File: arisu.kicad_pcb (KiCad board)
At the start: 2 copper layers, 339.1 x 118.7 mm, 176 parts, among them J1 USB_B_Micro, SW1 SW_Push, SW10 SW_Push, SW11 SW_Push, SW12 SW_Push, SW13 SW_Push, SW14 SW_Push, SW15 SW_Push, SW16 SW_Push, SW17 SW_Push, SW18 SW_Push, SW19 SW_Push, SW2 SW_Push, SW20 SW_Push, SW21 SW_Push, SW22 SW_Push, SW23 SW_Push, SW24 SW_Push, SW25 SW_Push, SW26 SW_Push, SW27 SW_Push, SW28 SW_Push, SW29 SW_Push, SW3 SW_Push, SW30 SW_Push, SW31 SW_Push, SW32 SW_Push, SW33 SW_Push, SW34 SW_Push, SW35 SW_Push, SW36 SW_Push, SW37 SW_Push, SW38 SW_Push, SW39 SW_Push, SW4 SW_Push, SW40 SW_Push, SW41 SW_Push, SW42 SW_Push, SW43 SW_Push, SW44 SW_Push, SW45 SW_Push, SW46 SW_Push, SW47 SW_Push, SW48 SW_Push, SW49 SW_Push, SW5 SW_Push, SW50 SW_Push, SW51 SW_Push, SW52 SW_Push, SW53 SW_Push, SW54 SW_Push, SW55 SW_Push, SW56 SW_Push, SW57 SW_Push, SW58 SW_Push, SW59 SW_Push, SW6 SW_Push, SW60 SW_Push, SW61 SW_Push, SW62 SW_Push, SW63 SW_Push, SW64 SW_Push, SW65 SW_Push, SW66 SW_Push, SW67 SW_Push, SW7 SW_Push, SW8 SW_Push, SW9 SW_Push, U1 USBLC6-2SC6, U2 ATmega32U4-AU, Y1 Crystal_GND24

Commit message: Begin reworking PCB layout with removed top row.
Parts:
- removed D1, D10, D15, D19, D24, D29, D33, D38, D42, D47, D51, D55, D59, D6, D63: D, Diodes_SMD:D_SOD-123
- removed G*** (x2): LOGO, arisu:arisu-logo
- removed SW1, SW10, SW15, SW19, SW24, SW29, SW33, SW38, SW42, SW47, SW51, SW55, SW59, SW6, SW63: SW_Push, Fate_Parts:SW_Cherry_MX_1.00u_PCB
- renumbered PF6 to J10, PF7 to J11, VCC to J12, D+ to J13, D- to J14, GND to J15, MISO to J2, VCC to J3, SCK to J4, MOSI to J5, RES to J6, GND to J7, PF4 to J8, PF5 to J9
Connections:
- D11 pad 1: /row1 -> /row0
- D12 pad 1: /row2 -> /row1
- D13 pad 1: /row3 -> /row2
- D14 pad 1: /row4 -> /row3
- D16 pad 1: /row1 -> /row0
- D17 pad 1: /row2 -> /row1
- D18 pad 1: /row3 -> /row2
- D2 pad 1: /row1 -> /row0
- D20 pad 1: /row1 -> /row0
- D21 pad 1: /row2 -> /row1
- D22 pad 1: /row3 -> /row2
- D23 pad 1: /row4 -> /row3
- D25 pad 1: /row1 -> /row0
- D26 pad 1: /row2 -> /row1
- D27 pad 1: /row3 -> /row2
- D28 pad 1: /row4 -> /row3
- D3 pad 1: /row2 -> /row1
- D30 pad 1: /row1 -> /row0
- D31 pad 1: /row2 -> /row1
- D32 pad 1: /row3 -> /row2
- D34 pad 1: /row1 -> /row0
- D35 pad 1: /row2 -> /row1
- D36 pad 1: /row3 -> /row2
- D37 pad 1: /row4 -> /row3
- D39 pad 1: /row1 -> /row0
- D4 pad 1: /row3 -> /row2
- D40 pad 1: /row2 -> /row1
- D41 pad 1: /row3 -> /row2
- D43 pad 1: /row1 -> /row0
- D44 pad 1: /row2 -> /row1
- D45 pad 1: /row3 -> /row2
- D46 pad 1: /row4 -> /row3
- D48 pad 1: /row1 -> /row0
- D49 pad 1: /row2 -> /row1
- D5 pad 1: /row4 -> /row3
- D50 pad 1: /row3 -> /row2
- D52 pad 1: /row1 -> /row0
- D53 pad 1: /row2 -> /row1
- D54 pad 1: /row3 -> /row2
- D56 pad 1: /row1 -> /row0
- D57 pad 1: /row2 -> /row1
- D58 pad 1: /row4 -> /row3
- D60 pad 1: /row1 -> /row0
- D61 pad 1: /row3 -> /row2
- D62 pad 1: /row4 -> /row3
- D64 pad 1: /row1 -> /row0
- D65 pad 1: /row2 -> /row1
- D66 pad 1: /row3 -> /row2
- D67 pad 1: /row4 -> /row3
- D7 pad 1: /row1 -> /row0
- D8 pad 1: /row2 -> /row1
- D9 pad 1: /row3 -> /row2
- U2 pad 22: /row4 -> Net-(U2-Pad22)
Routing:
- net Net-(D42-Pad2): track 5.08 -> 0.00 mm
- net Net-(D38-Pad2): track 5.08 -> 0.00 mm
- net Net-(D33-Pad2): track 5.08 -> 0.00 mm
- net Net-(D47-Pad2): track 5.08 -> 0.00 mm
- net Net-(D51-Pad2): track 4.91 -> 0.00 mm
- net Net-(D10-Pad2): track 4.91 -> 0.00 mm
- net Net-(D6-Pad2): track 4.91 -> 0.00 mm
- net Net-(D1-Pad2): track 4.91 -> 0.00 mm
- net Net-(D63-Pad2): track 4.91 -> 0.00 mm
- net Net-(D59-Pad2): track 4.91 -> 0.00 mm
- net Net-(D55-Pad2): track 4.91 -> 0.00 mm
- net Net-(D29-Pad2): track 4.85 -> 0.00 mm
- net Net-(D24-Pad2): track 4.85 -> 0.00 mm
- net Net-(D19-Pad2): track 4.85 -> 0.00 mm
- net Net-(D15-Pad2): track 4.85 -> 0.00 mm
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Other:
- board text added: "Faux Design Rev 0.0.0"
- board text removed: "Fate Design Rev 1.1"

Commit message: Redesign alpha layout for natural finger spread.
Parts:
- removed D60, D64, D65, D66, D67: D, Diodes_SMD:D_SOD-123
- removed SW60: SW_Push, Fate_Parts:SW_Cherry_MX_1.50u_PCB
- removed SW64, SW65, SW66, SW67: SW_Push, Fate_Parts:SW_Cherry_MX_1.00u_PCB
- moved SW25 160.0 mm to (162.0, 217.3), turned to 344 degrees
- moved D25 159.9 mm to (164.0, 231.6), turned to 74 degrees
- moved SW20 158.8 mm to (143.7, 212.1), turned to 344 degrees
- moved D20 158.8 mm to (147.1, 226.4), turned to 74 degrees
- moved SW30 157.1 mm to (192.0, 222.6), turned to 16 degrees
- moved D30 156.6 mm to (201.7, 233.6), turned to 106 degrees
- moved SW31 156.0 mm to (206.4, 238.3), turned to 16 degrees
- moved SW34 155.8 mm to (210.3, 217.3), turned to 16 degrees
- moved D34 155.7 mm to (220.1, 228.8), turned to 106 degrees
- moved D26 155.2 mm to (150.1, 247.7), turned to 74 degrees
- moved D32 155.1 mm to (229.7, 265.6), turned to 106 degrees
- moved SW32 155.1 mm to (220.8, 253.9), turned to 16 degrees
- moved D31 155.0 mm to (216.2, 248.8), turned to 106 degrees
- moved SW26 154.8 mm to (147.6, 233.0), turned to 344 degrees
- moved D35 154.8 mm to (234.2, 244.7), turned to 106 degrees
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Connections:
- J1 pad 4: Net-(J1-Pad4) -> (no net)
- SW61 pad 1: /col13 -> /col12
- SW62 pad 1: /col13 -> /col11
- U1 pad 1: Net-(U1-Pad1) -> (no net)
- U1 pad 3: Net-(U1-Pad3) -> (no net)
- U2 pad 22: Net-(U2-Pad22) -> (no net)
- U2 pad 26: /col13 -> (no net)
- U2 pad 42: Net-(U2-Pad42) -> (no net)
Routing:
- net /row4: track 433.8 -> 0.00 mm, vias 2 -> 0
- net /row3: track 432.5 -> 0.00 mm, vias 2 -> 0
- net /row2: track 399.4 -> 0.00 mm, vias 4 -> 0
- net /row1: track 384.1 -> 0.00 mm, vias 4 -> 0
- net /row0: track 328.0 -> 0.00 mm, vias 4 -> 0
- net /MISO: track 272.2 -> 0.00 mm, vias 1 -> 0
- net /col13: track 269.0 -> 0.00 mm
- net /col12: track 249.0 -> 0.00 mm
- net /col11: track 230.6 -> 0.00 mm
- net /col10: track 221.3 -> 0.00 mm
- net VCC: track 205.4 -> 0.00 mm, vias 9 -> 0
- net /col0: track 204.9 -> 0.00 mm, vias 1 -> 0
- net /col2: track 175.7 -> 0.00 mm, vias 2 -> 0
- net /col1: track 166.8 -> 0.00 mm
- net /SCK: track 157.0 -> 0.00 mm, vias 2 -> 0
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
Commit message: Continue making symmetrical layout.
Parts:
- moved D28 158.5 mm to (149.7, 292.2)
- moved SW28 158.5 mm to (146.3, 277.9)
- moved D46 157.6 mm to (272.3, 278.3)
- moved SW37 157.6 mm to (207.4, 278.5)
- moved SW46 157.6 mm to (258.7, 267.6)
- moved D37 157.6 mm to (232.7, 286.7)
- moved SW23 157.5 mm to (105.4, 268.8)
- moved D23 157.5 mm to (118.2, 285.1)
- moved SW14 151.4 mm to (47.1, 251.8), turned to 0 degrees
- moved D11 150.3 mm to (97.7, 211.1)
- moved SW11 150.3 mm to (94.3, 196.8)
- moved D16 150.3 mm to (116.4, 215.1)
- moved SW16 150.3 mm to (113.0, 200.8)
- moved D14 148.9 mm to (57.7, 265.2), turned to 90 degrees
- moved D12 148.0 mm to (89.1, 228.8)
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
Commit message: Make 69 spacebar layout lol.
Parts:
- removed D61: D, Diodes_SMD:D_SOD-123
- removed SW61: SW_Push, Fate_Parts:SW_Cherry_MX_1.00u_PCB
- added D63: D, Diode_SMD:D_SOD-123, B.Cu at (348.3, 111.3)
- added D64: D, Diode_SMD:D_SOD-123, F.Cu at (375.0, 54.8)
- added D69: D, Diode_SMD:D_SOD-123, F.Cu at (203.6, 154.8)
- added SW63: SW_Push, MX_Switch:SW_Cherry_MX_1.00u_PCB, F.Cu at (342.4, 98.3)
- added SW64: SW_Push, MX_Switch:SW_Cherry_MX_1.00u_PCB, F.Cu at (369.4, 41.1)
- added SW69: SW_Push, Button_Switch_Keyboard:SW_Cherry_MX_6.25u_PCB, F.Cu at (209.6, 146.4)
- SW11, SW12, SW13, SW16, SW17, SW18, SW20, SW21, SW22, SW25, SW26, SW27, SW30, SW31, SW32, SW34, SW35, SW36, SW39, SW40, SW41, SW43, SW44, SW45, SW48, SW49, SW50, SW52, SW53, SW56, SW7, SW8, SW9: footprint Fate_Parts:SW_Cherry_MX_1.00u_PCB -> MX_Switch:SW_Cherry_MX_1.00u_PCB
- SW14, SW2, SW46, SW5: footprint Fate_Parts:SW_Cherry_MX_1.50u_PCB -> MX_Switch:SW_Cherry_MX_1.50u_PCB
- SW23: footprint Fate_Parts:SW_Cherry_MX_2.00u_PCB_ReversedStabilizers -> MX_Switch:SW_Cherry_MX_1.00u_PCB
- SW28: footprint Fate_Parts:SW_Cherry_MX_1.00u_PCB -> MX_Switch:SW_Cherry_MX_2.25u_PCB_ReversedStabilizers
- SW3: footprint Fate_Parts:SW_Cherry_MX_1.75u_PCB -> MX_Switch:SW_Cherry_MX_1.75u_PCB
- SW37: footprint Fate_Parts:SW_Cherry_MX_2.75u_PCB_ReversedStabilizers -> MX_Switch:SW_Cherry_MX_2.25u_PCB_ReversedStabilizers
- SW4: footprint Fate_Parts:SW_Cherry_MX_2.25u_PCB -> MX_Switch:SW_Cherry_MX_2.25u_PCB
- SW54: footprint Fate_Parts:SW_Cherry_MX_1.75u_PCB -> MX_Switch:SW_Cherry_MX_2.75u_PCB
- SW57: footprint Fate_Parts:SW_Cherry_MX_2.25u_PCB_ReversedStabilizers -> MX_Switch:SW_Cherry_MX_2.25u_PCB_ReversedStabilizers
- SW58, SW62: footprint Fate_Parts:SW_Cherry_MX_1.00u_PCB -> MX_Switch:SW_Cherry_MX_1.50u_PCB
- moved SW28 163.9 mm to (148.8, 114.0)
- moved D28 162.1 mm to (163.1, 130.7)
- moved D23 161.5 mm to (133.8, 124.3)
- moved SW23 160.7 mm to (130.2, 110.0)
- moved D54 157.4 mm to (360.8, 92.5)
- moved SW37 156.0 mm to (219.6, 122.9)
- moved D12 155.9 mm to (108.2, 74.0)
- moved D13 155.9 mm to (99.6, 91.6)
- moved D14 155.9 mm to (76.8, 110.4)
- moved D16 155.9 mm to (135.4, 60.3)
- moved D17 155.9 mm to (126.8, 78.0)
- moved D18 155.9 mm to (118.2, 95.6)
- moved D2 155.9 mm to (61.9, 53.1)
- moved D20 155.9 mm to (164.3, 71.6)
- moved D21 155.9 mm to (150.5, 87.3)
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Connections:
- SW46 pad 1: /col9 -> /col8
- SW62 pad 1: /col11 -> /col9
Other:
- board size 339.1 x 118.7 mm -> 373.1 x 131.8 mm
- board text added: "Faux Keebs Rev 0.0.0"
- board text removed: "Faux Design Rev 0.0.0"

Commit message: Make it even MORE symmetrical!
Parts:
- removed D69: D, Diode_SMD:D_SOD-123
- removed SW69: SW_Push, Button_Switch_Keyboard:SW_Cherry_MX_6.25u_PCB
- moved H6 51.9 mm to (226.2, 131.0)
- moved H4 44.2 mm to (184.5, 131.0)
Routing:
- net /SCK: track 0.00 -> 105.4 mm
- net /col2: track 0.00 -> 89.6 mm
- net /col12: track 0.00 -> 86.2 mm
- net /col8: track 0.00 -> 86.1 mm
- net /col10: track 0.00 -> 84.0 mm
- net /col5: track 0.00 -> 82.3 mm
- net /col9: track 0.00 -> 81.7 mm
- net /col4: track 0.00 -> 81.0 mm
- net /col0: track 0.00 -> 80.1 mm
- net /col1: track 0.00 -> 53.3 mm
- net /col3: track 0.00 -> 52.1 mm
- net /col11: track 0.00 -> 50.9 mm
- net /col6: track 0.00 -> 47.2 mm
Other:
- board size 373.1 x 131.8 mm -> 373.1 x 110.3 mm

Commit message: Route more row tracks.
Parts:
- moved D64 0.89 mm to (375.9, 54.6)
- moved D58 0.65 mm to (372.1, 111.6)
- turned D63 to 90 degrees
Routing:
- net /row1: track 0.00 -> 373.1 mm
- net /row3: track 0.00 -> 370.3 mm
- net /row0: track 0.00 -> 349.7 mm
- net Net-(D32-Pad2): track 0.00 -> 5.79 mm
- net Net-(D36-Pad2): track 0.00 -> 5.74 mm
- net Net-(D35-Pad2): track 0.00 -> 5.64 mm
- net Net-(D22-Pad2): track 0.00 -> 5.36 mm
- net Net-(D44-Pad2): track 0.00 -> 5.33 mm
- net Net-(D37-Pad2): track 0.00 -> 5.27 mm
- net Net-(D34-Pad2): track 0.00 -> 5.24 mm
- net Net-(D41-Pad2): track 0.00 -> 5.23 mm
- net Net-(D64-Pad2): track 0.00 -> 5.23 mm
- net Net-(D43-Pad2): track 0.00 -> 5.21 mm
- net Net-(D30-Pad2): track 0.00 -> 5.11 mm
- net Net-(D26-Pad2): track 0.00 -> 5.09 mm
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
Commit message: Finish routing rows.
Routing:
- net /row2: track 0.00 -> 420.6 mm
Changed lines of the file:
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@@
     (thickness 1.6)
     (drawings 1381)
-    (tracks 397)
+    (tracks 458)
     (zones 0)
     (modules 136)
@@
   (segment (start 56.384333 66.445157) (end 55.799333 65.860157) (width 0.25) (layer B.Cu) (net 9))
   (segment (start 56.384333 70.525157) (end 56.384333 66.445157) (width 0.25) (layer B.Cu) (net 9))
+  (segment (start 375.92 65.172491) (end 375.92 56.26) (width 0.25) (layer B.Cu) (net 10))
+  (segment (start 123.19 101.6) (end 127 104.14) (width 0.25) (layer B.Cu) (net 10))
+  (segment (start 79.410583 92.875157) (end 79.410583 93.575157) (width 0.25) (layer B.Cu) (net 10))
+  (segment (start 378.46 67.712491) (end 375.92 65.172491) (width 0.25) (layer B.Cu) (net 10))
+  (segment (start 378.46 85.09) (end 378.46 67.712491) (width 0.25) (layer B.Cu) (net 10))
+  (segment (start 79.410583 93.575157) (end 81.085426 95.25) (width 0.25) (layer B.Cu) (net 10))
+  (segment (start 269.24 109.22) (end 280.93211 105.14789) (width 0.25) (layer B.Cu) (net 10))
+  (segment (start 345.44 96.52) (end 348.903637 93.633637) (width 0.25) (layer B.Cu) (net 10))
+  (segment (start 359.41 96.52) (end 369.57 96.52) (width 0.25) (layer B.Cu) (net 10))
+  (segment (start 348.903637 93.633637) (end 356.523637 93.633637) (width 0.25) (layer B.Cu) (net 10))
+  (segment (start 356.523637 93.633637) (end 359.41 96.52) (width 0.25) (layer B.Cu) (net 10))
+  (segment (start 369.57 96.52) (end 378.46 85.09) (width 0.25) (layer B.Cu) (net 10))
+  (segment (start 360.76089 95.16911) (end 359.41 96.52) (width 0.25) (layer B.Cu) (net 10))
+  (segment (start 360.76089 94.151218) (end 360.76089 95.16911) (width 0.25) (layer B.Cu) (net 10))
+  (segment (start 324.706479 94.151218) (end 322.337697 96.52) (width 0.25) (layer B.Cu) (net 10))
+  (segment (start 324.856479 94.151218) (end 324.706479 94.151218) (width 0.25) (layer B.Cu) (net 10))
+  (segment (start 322.337697 96.52) (end 320.04 96.52) (width 0.25) (layer B.Cu) (net 10))
+  (segment (start 320.04 96.52) (end 323.85 96.52) (width 0.25) (layer B.Cu) (net 10))
+  (segment (start 318.77 96.52) (end 323.85 96.52) (width 0.25) (layer B.Cu) (net 10))
+  (segment (start 323.85 96.52) (end 345.44 96.52) (width 0.25) (layer B.Cu) (net 10))
+  (segment (start 306.215179 96.086687) (end 308.899246 98.770754) (width 0.25) (layer B.Cu) (net 10))
+  (segment (start 304.611595 96.086687) (end 306.215179 96.086687) (width 0.25) (layer B.Cu) (net 10))
+  (segment (start 308.899246 98.770754) (end 318.77 96.52) (width 0.25) (layer B.Cu) (net 10))
+  (segment (start 285.977885 103.764403) (end 285.676144 104.066144) (width 0.25) (layer B.Cu) (net 10))
+  (segment (start 285.977885 100.047407) (end 285.977885 103.764403) (width 0.25) (layer B.Cu) (net 10))
+  (segment (start 280.93211 105.14789) (end 285.676144 104.066144) (width 0.25) (layer B.Cu) (net 10))
+  (segment (start 285.676144 104.066144) (end 308.899246 98.770754) (width 0.25) (layer B.Cu) (net 10))
+  (segment (start 265.229474 109.284883) (end 265.229474 110.289474) (width 0.25) (layer B.Cu) (net 10))
+  (segment (start 267.117263 107.397094) (end 265.229474 109.284883) (width 0.25) (layer B.Cu) (net 10))
+  (segment (start 267.841442 107.397094) (end 267.117263 107.397094) (width 0.25) (layer B.Cu) (net 10))
+  (segment (start 250.19 114.3) (end 265.229474 110.289474) (width 0.25) (layer B.Cu) (net 10))
+  (segment (start 265.229474 110.289474) (end 269.24 109.22) (width 0.25) (layer B.Cu) (net 10))
+  (segment (start 248.92 113.32333) (end 248.92 114.3) (width 0.25) (layer B.Cu) (net 10))
+  (segment (start 249.234402 113.008928) (end 248.92 113.32333) (width 0.25) (layer B.Cu) (net 10))
+  (segment (start 249.234402 112.440794) (end 249.234402 113.008928) (width 0.25) (layer B.Cu) (net 10))
+  (segment (start 162.56 114.3) (end 248.92 114.3) (width 0.25) (layer B.Cu) (net 10))
+  (segment (start 248.92 114.3) (end 250.19 114.3) (width 0.25) (layer B.Cu) (net 10))
+  (segment (start 153.733802 111.696198) (end 153.67 111.76) (width 0.25) (layer B.Cu) (net 10))
+  (segment (start 153.733802 109.821239) (end 153.733802 111.696198) (width 0.25) (layer B.Cu) (net 10))
+  (segment (start 153.67 111.76) (end 162.56 114.3) (width 0.25) (layer B.Cu) (net 10))
+  (segment (start 133.492318 105.267682) (end 132.926667 105.833333) (width 0.25) (layer B.Cu) (net 10))
+  (segment (start 134.57291 105.267682) (end 133.492318 105.267682) (width 0.25) (layer B.Cu) (net 10))
+  (segment (start 135.007432 104.83316) (end 134.57291 105.267682) (width 0.25) (layer B.Cu) (net 10))
+  (segment (start 127 104.14) (end 132.926667 105.833333) (width 0.25) (layer B.Cu) (net 10))
+  (segment (start 132.926667 105.833333) (end 153.67 111.76) (width 0.25) (layer B.Cu) (net 10))
+  (segment (start 118.11 98.051624) (end 118.11 100.33) (width 0.25) (layer B.Cu) (net 10))
+  (segment (start 117.837529 97.779153) (end 118.11 98.051624) (width 0.25) (layer B.Cu) (net 10))
+  (segment (start 117.837529 97.219101) (end 117.837529 97.779153) (width 0.25) (layer B.Cu) (net 10))
+  (segment (start 97.79 95.25) (end 118.11 100.33) (width 0.25) (layer B.Cu) (net 10))
+  (segment (start 118.11 100.33) (end 123.19 101.6) (width 0.25) (layer B.Cu) (net 10))
+  (segment (start 97.21663 95.25) (end 96.52 95.25) (width 0.25) (layer B.Cu) (net 10))
+  (segment (start 99.207529 93.259101) (end 97.21663 95.25) (width 0.25) (layer B.Cu) (net 10))
+  (segment (start 81.085426 95.25) (end 96.52 95.25) (width 0.25) (layer B.Cu) (net 10))
+  (segment (start 96.52 95.25) (end 97.79 95.25) (width 0.25) (layer B.Cu) (net 10))
+  (segment (start 81.085426 95.25) (end 68.58 95.25) (width 0.25) (layer B.Cu) (net 10))
+  (segment (start 68.58 95.25) (end 64.77 91.44) (width 0.25) (layer B.Cu) (net 10))
+  (segment (start 64.77 91.44) (end 60.96 91.44) (width 0.25) (layer B.Cu) (net 10))
+  (segment (start 60.96 91.44) (end 57.15 95.25) (width 0.25) (layer B.Cu) (net 10))
+  (segment (start 57.15 95.25) (end 49.53 95.25) (width 0.25) (layer B.Cu) (net 10))
+  (segment (start 48.456833 94.176833) (end 48.456833 92.875157) (width 0.25) (layer B.Cu) (net 10))
+  (segment (start 49.53 95.25) (end 48.456833 94.176833) (width 0.25) (layer B.Cu) (net 10))
   (segment (start 48.606833 111.925157) (end 50.981676 114.3) (width 0.25) (layer B.Cu) (net 11))
   (segment (start 48.456833 111.925157) (end 48.606833 111.925157) (width 0.25) (layer B.Cu) (net 11))

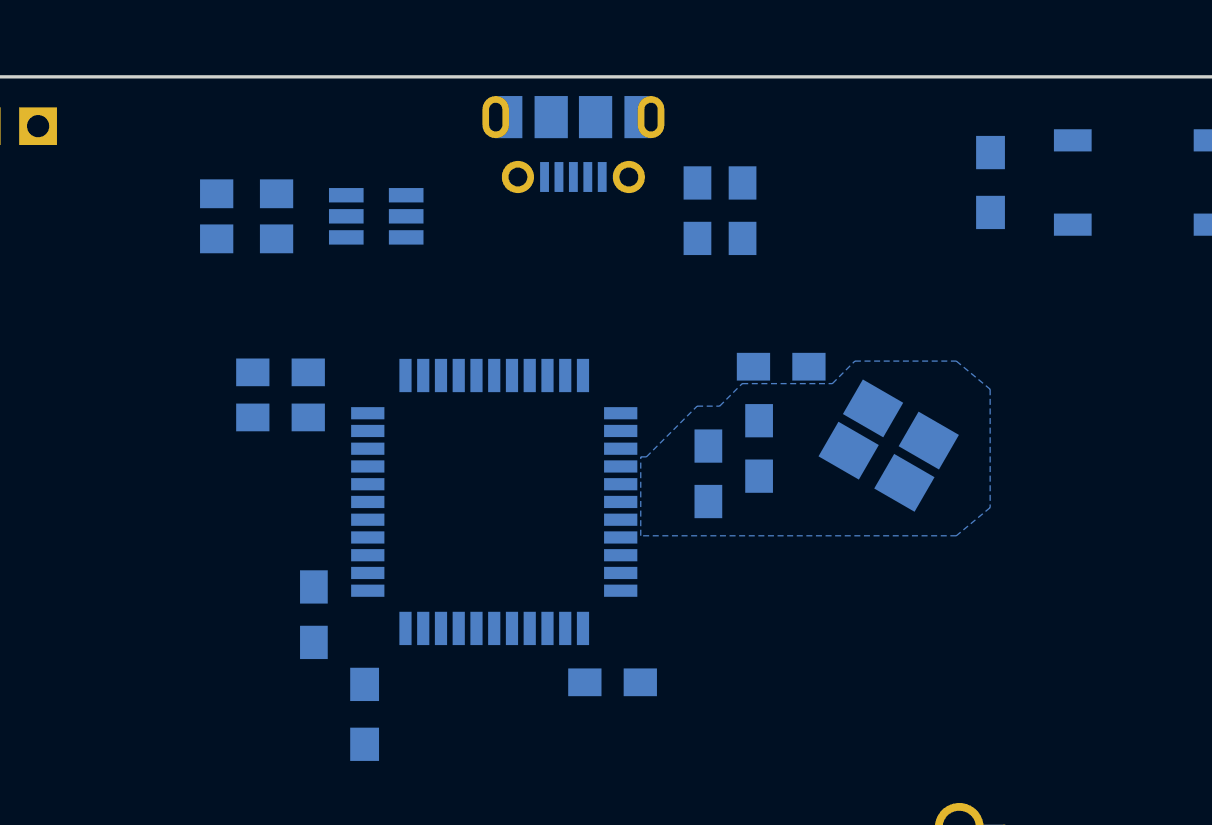
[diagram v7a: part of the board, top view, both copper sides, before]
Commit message: Route some of the central components.
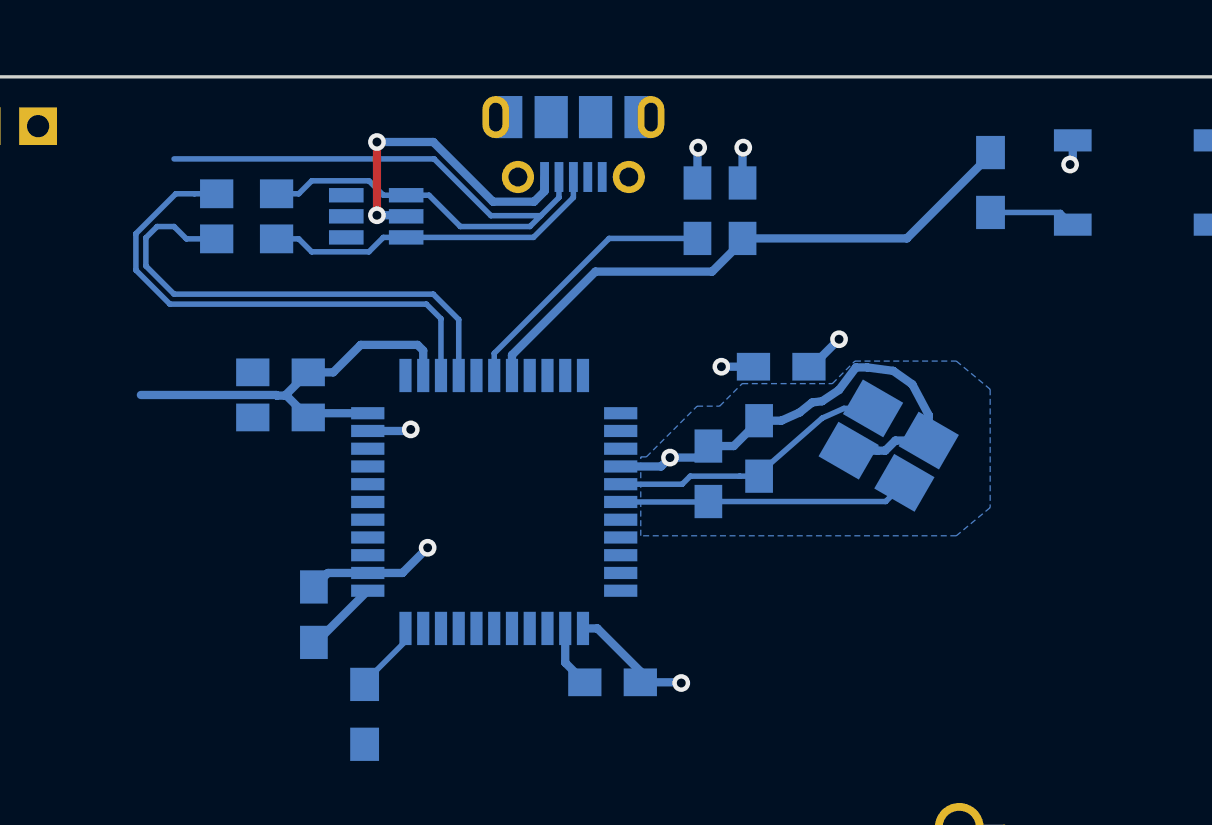
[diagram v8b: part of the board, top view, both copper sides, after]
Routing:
- net VCC: track 0.00 -> 67.3 mm, vias 0 -> 3
- net GND: track 0.00 -> 41.4 mm, vias 0 -> 8
- net Net-(J1-Pad2): track 0.00 -> 32.9 mm
- net D-: track 0.00 -> 23.2 mm
- net D+: track 0.00 -> 22.5 mm
- net Net-(J1-Pad3): track 0.00 -> 15.6 mm
- net XTAL1: track 0.00 -> 13.1 mm
- net XTAL2: track 0.00 -> 12.7 mm
- net Net-(C4-Pad1): track 0.00 -> 12.3 mm
- net /~RES~: track 0.00 -> 3.94 mm
- net Net-(R4-Pad1): track 0.00 -> 3.28 mm
